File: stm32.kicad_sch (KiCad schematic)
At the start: 30 parts, among them J2 Micro_SD_Card, U1 STM32F103VETx, Y101 8MHz, Y102 32.768KHz

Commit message: Znacajne izmene seme
Dodao prikljucak za UV senzor
Dodao reset za GPS
Dodao ext_ant za GPS
Dodao 3D modele
Dodao testpoint-e
Sredio semu malo
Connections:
- net UV: now reaches U1.23 (PA0)
- net GPS_RESET: now reaches U1.67 (PA8)
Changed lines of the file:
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@@
+		)
+	)
+	(global_label "UV"
+		(shape input)
+		(at 27.94 168.91 180)
+		(fields_autoplaced yes)
+		(effects
+			(font
+				(size 1.27 1.27)
+			)
+			(justify right)
+		)
+		(property "Intersheetrefs" "${INTERSHEET_REFS}"
+			(at 22.5357 168.91 0)
+			(effects
+				(font
+					(size 1.27 1.27)
+				)
+				(justify right)
+				(hide yes)
+			)
 		)
 	)
@@
 			(effects
 				(font
+					(size 1.27 1.27)
+				)
+				(justify right)
+				(hide yes)
+			)
+		)
+	)
+	(global_label "GPS_RESET"
+		(shape input)
+		(at 27.94 148.59 180)
+		(fields_autoplaced yes)
+		(effects
+			(font
+				(size 1 1)
+			)
+			(justify right)
+		)
+		(property "Intersheetrefs" "${INTERSHEET_REFS}"
+			(at 17.3515 148.59 0)
+			(effects
+				(font

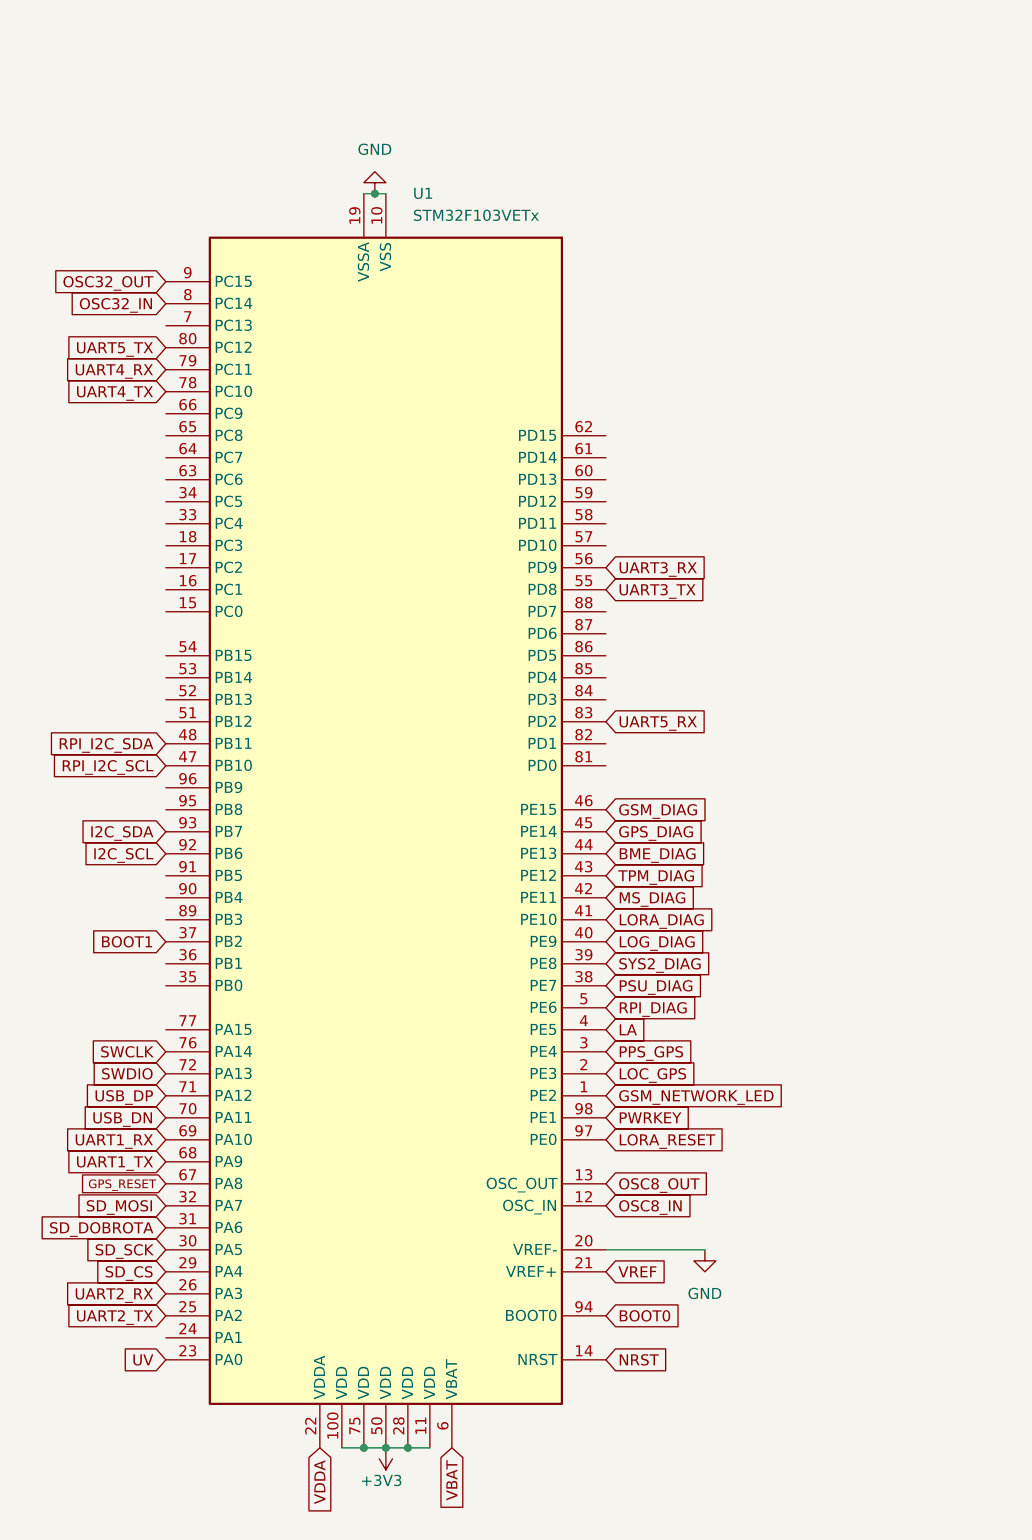
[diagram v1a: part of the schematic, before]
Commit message: Znacajne izmene seme i pcb-a
Napravljen nov layout
dodat konektor za gpio
dodat konektor za eksterna merenja vetra
izmenjene diag lampice
izmenjen konektor za ext plocu
razno
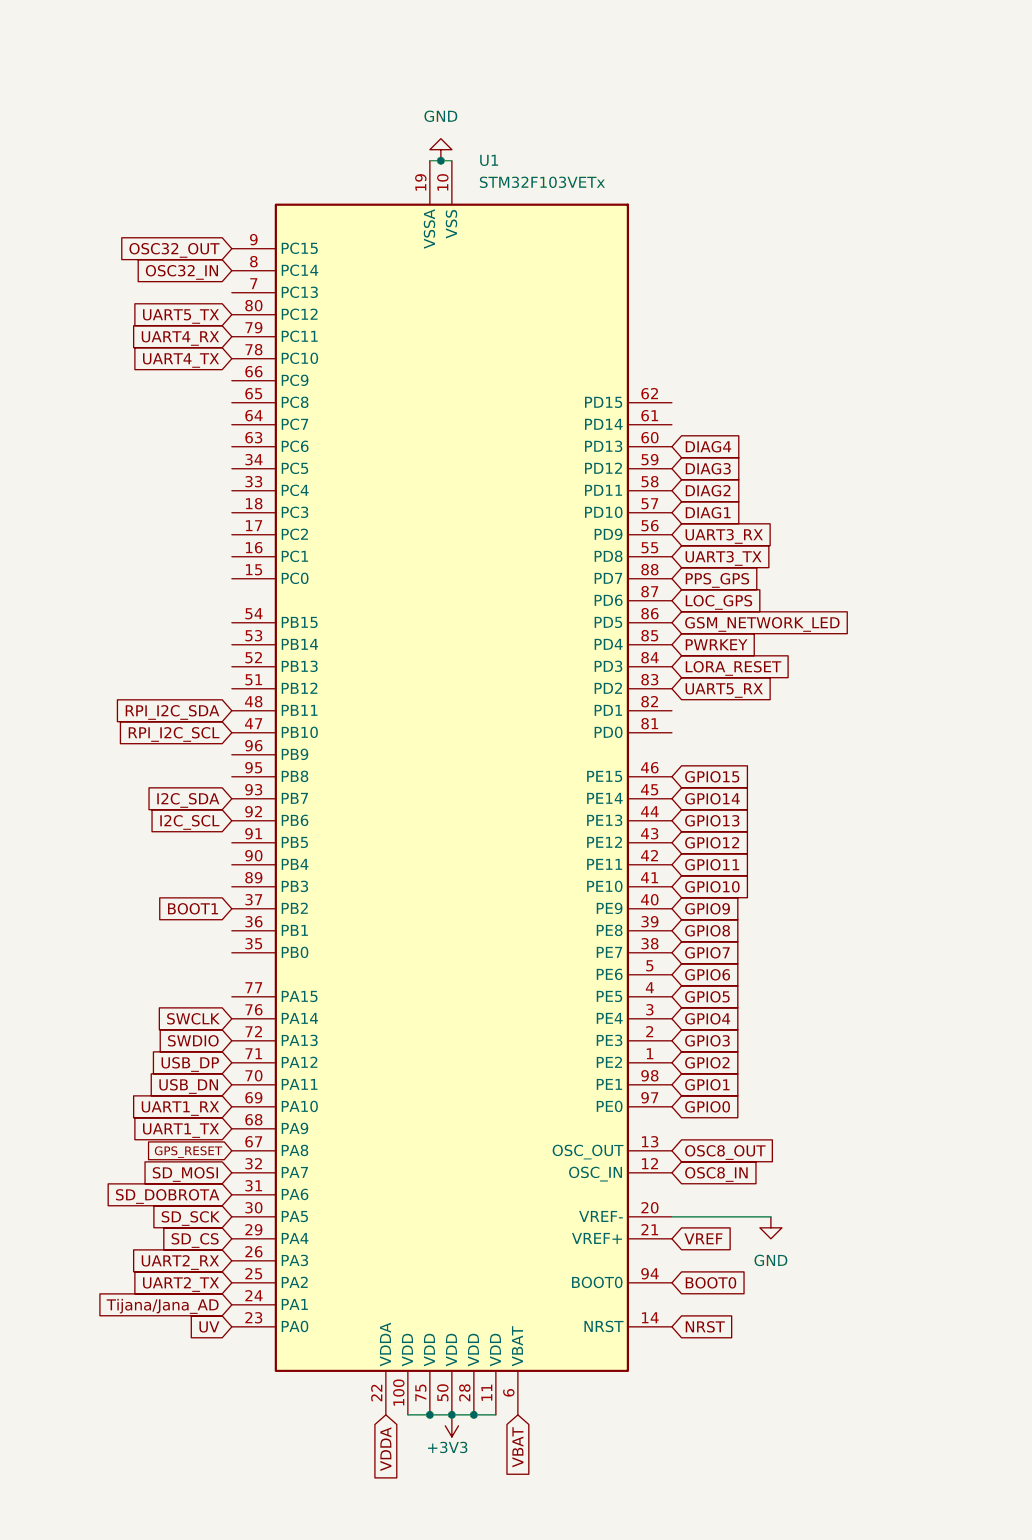
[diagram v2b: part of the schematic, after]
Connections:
- net GSM_NETWORK_LED: now also U1.86 (PD5); no longer U1.1 (PE2)
- net LOC_GPS: now also U1.87 (PD6); no longer U1.2 (PE3)
- net LORA_RESET: now also U1.84 (PD3); no longer U1.97 (PE0)
- net PPS_GPS: now also U1.88 (PD7); no longer U1.3 (PE4)
- net PWRKEY: now also U1.85 (PD4); no longer U1.98 (PE1)
- net Tijana/Jana_AD: now reaches U1.24 (PA1)
- net DIAG1: now reaches U1.57 (PD10)
- net DIAG2: now reaches U1.58 (PD11)
- net DIAG3: now reaches U1.59 (PD12)
- net DIAG4: now reaches U1.60 (PD13)
- net BME_DIAG renamed GPIO13
- net GPS_DIAG renamed GPIO14
- net GSM_DIAG renamed GPIO15
- net LA renamed GPIO5
- net LOG_DIAG renamed GPIO9
- net LORA_DIAG renamed GPIO10
- net MS_DIAG renamed GPIO11
- net PSU_DIAG renamed GPIO7
- net RPI_DIAG renamed GPIO6
- net SYS2_DIAG renamed GPIO8
- net TPM_DIAG renamed GPIO12
- new net GPIO0: U1.97 (PE0)
- new net GPIO1: U1.98 (PE1)
- new net GPIO2: U1.1 (PE2)
- new net GPIO3: U1.2 (PE3)
- new net GPIO4: U1.3 (PE4)
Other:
- moved on the sheet: U1

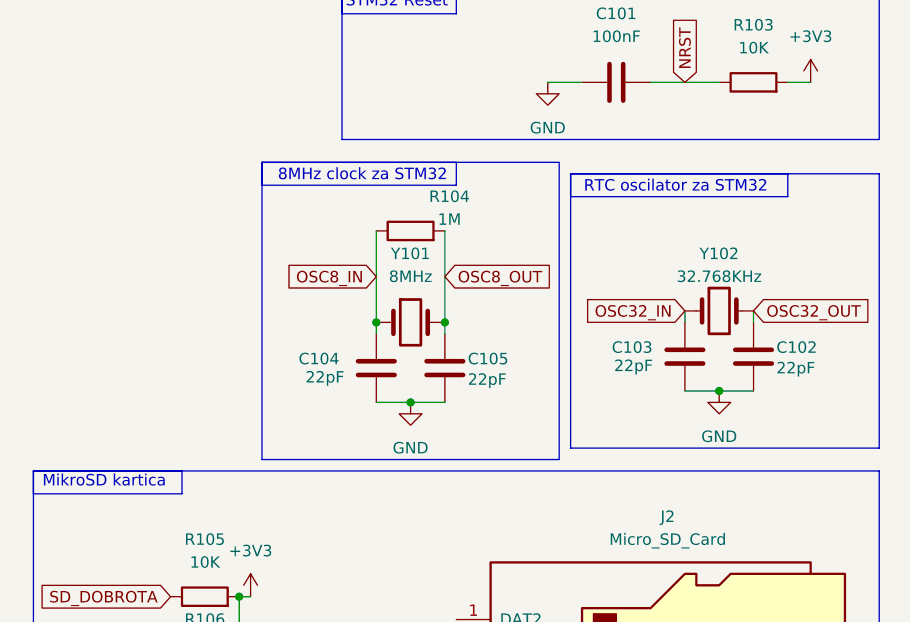
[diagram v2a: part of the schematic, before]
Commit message: Velike izmene PCB
Zavrsena mala spoljanja plocica
Preliminarni placement komponenti na velikoj plocici
Dodati logotipi ISP i ELE
Dodato potpise
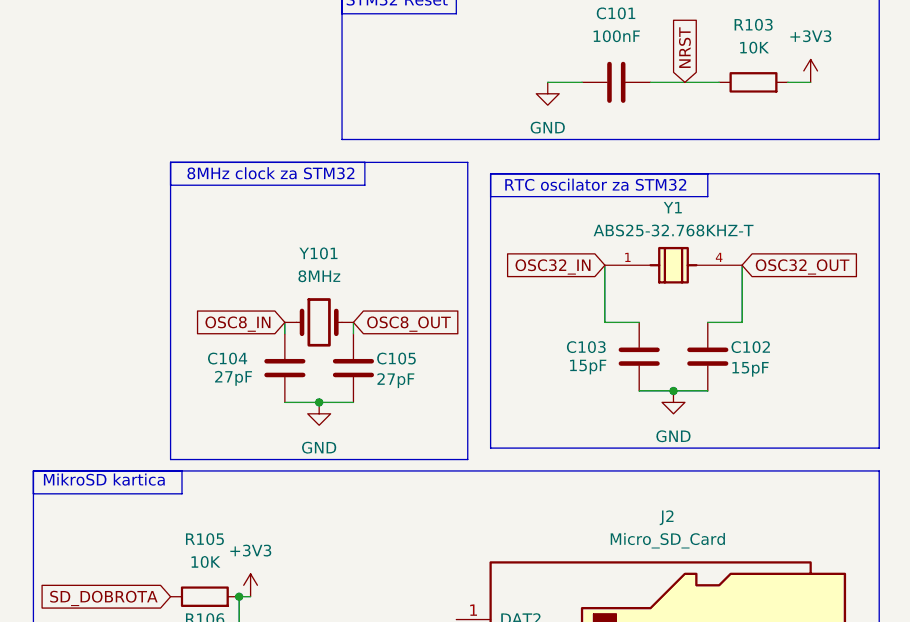
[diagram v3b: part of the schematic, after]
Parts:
- removed R104: 1M, Resistor_SMD:R_1206_3216Metric_Pad1.30x1.75mm_HandSolder, symbol Device:R
- removed Y102: 32.768KHz, Crystal:Crystal_HC49-U_Vertical, symbol Device:Crystal
- added Y1: ABS25-32.768KHZ-T, Crystal:Crystal_SMD_Abracon_ABS25-4Pin_8.0x3.8mm, symbol ABS25-32.768KHZ-T:ABS25-32.768KHZ-T
- C102, C103: value 22pF -> 15pF
- C104, C105: value 22pF -> 27pF
- Y101: footprint Crystal:Crystal_HC49-U_Vertical -> Crystal:Crystal_SMD_HC49-SD
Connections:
- net OSC32_IN: now also Y1.1
- net OSC32_OUT: now also Y1.4
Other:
- moved on the sheet: C102, C103, C104, C105, Y101
